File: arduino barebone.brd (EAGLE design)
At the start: 64.8 x 75.9 mm, 20 parts

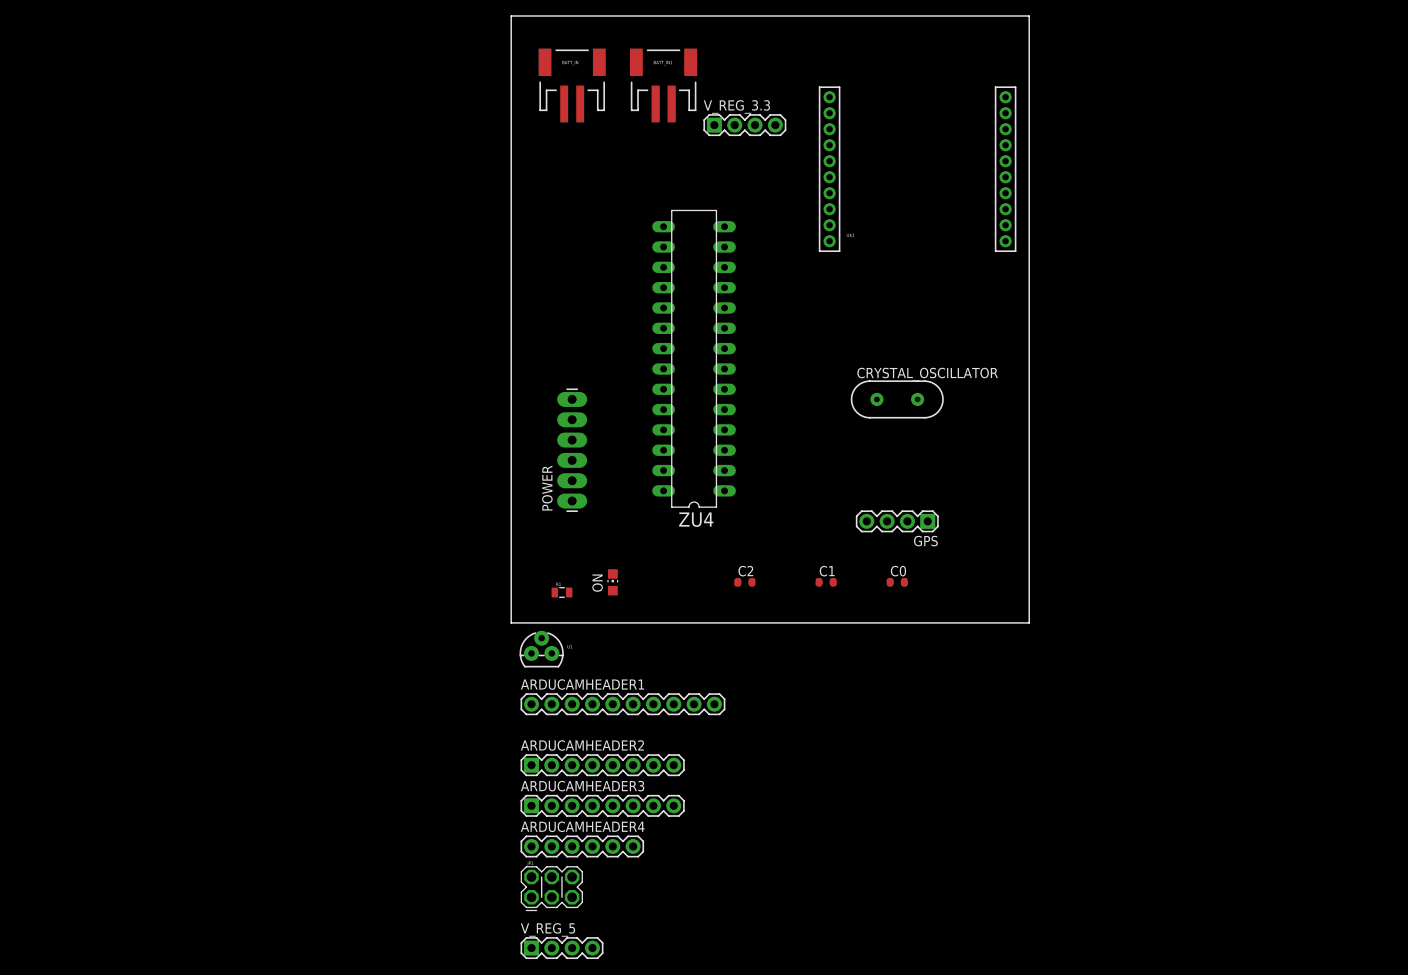
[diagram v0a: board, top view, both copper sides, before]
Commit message: started placing components. arduino shield layout
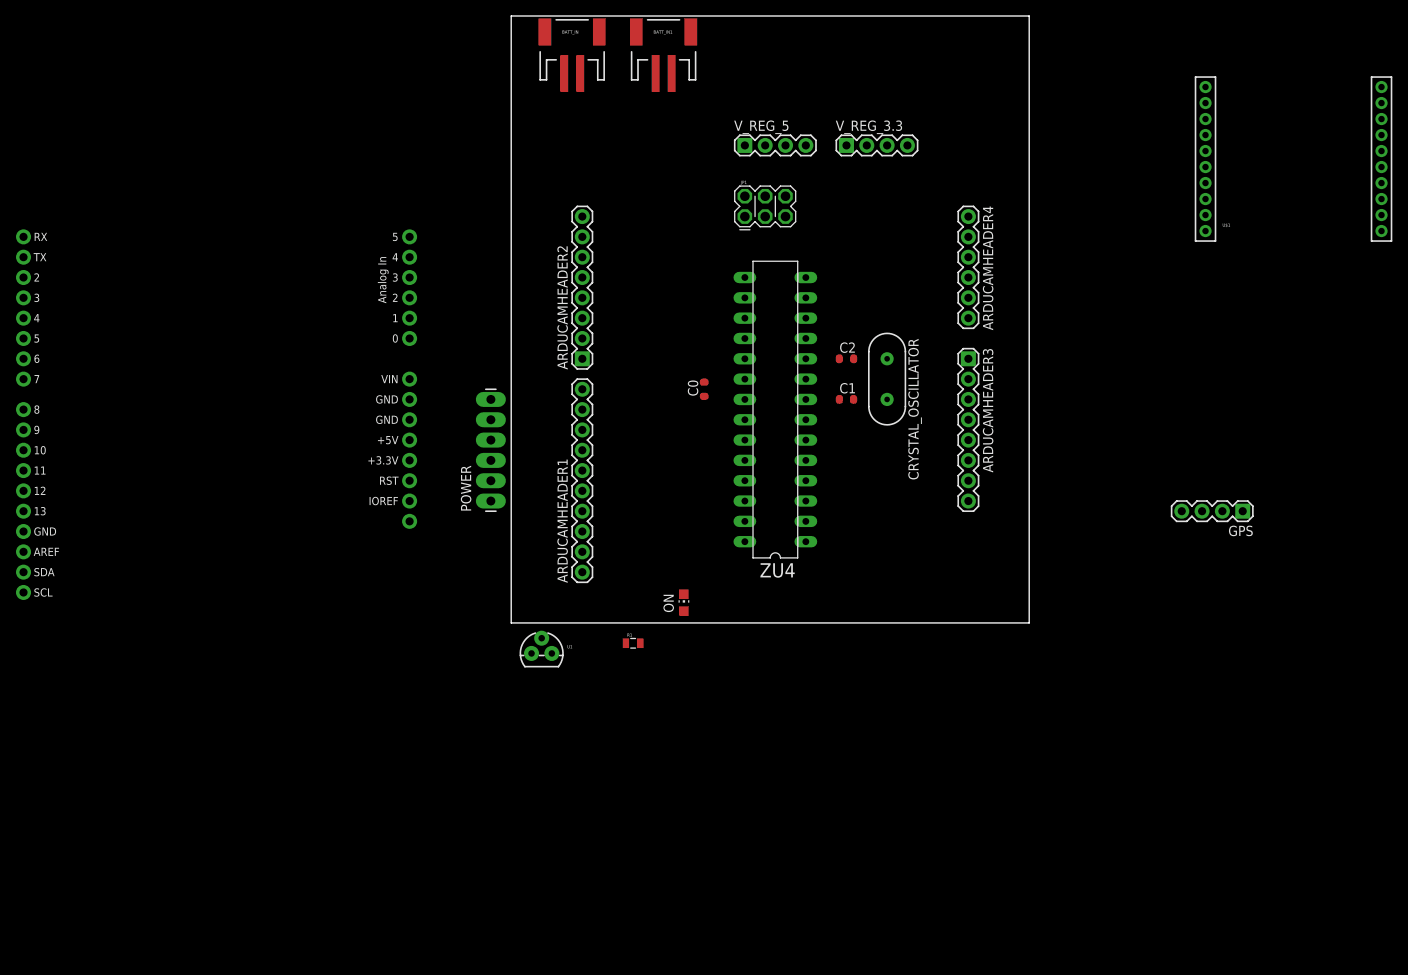
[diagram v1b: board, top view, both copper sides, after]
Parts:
- added U$2: ARDUINO_R3_SHIELD, SparkFun-Boards:UNO_R3_SHIELD
- moved V_REG_5 103.8 mm to (29.2, 59.7)
- moved ARDUCAMHEADER4 95.8 mm to (57.1, 50.8), turned to 270 degrees
- moved JP1 89.2 mm to (29.2, 50.8)
- moved ARDUCAMHEADER3 78.1 mm to (57.1, 33.0), turned to 270 degrees
- moved ARDUCAMHEADER2 51.2 mm to (8.89, 33.0), turned to 90 degrees
- moved U$1 47.0 mm to (97.8, 47.0)
- moved GPS 39.4 mm to (91.4, 14.0)
- moved C0 34.1 mm to (24.1, 29.2), turned to 90 degrees
- moved C2 30.7 mm to (41.9, 33.0)
- moved C1 23.0 mm to (41.9, 27.9)
- moved ARDUCAMHEADER1 17.7 mm to (8.89, 6.35), turned to 90 degrees
- moved V_REG_3.3 16.7 mm to (41.9, 59.7)
- moved ZU4 12.0 mm to (33.0, 26.7)
- moved R1 10.9 mm to (15.2, -2.54)
- moved POWER 10.2 mm to (-2.54, 15.2)
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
